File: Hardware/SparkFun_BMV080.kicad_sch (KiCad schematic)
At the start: 27 parts, among them J2 Qwiic_Vertical, J3 Conn_01x06, J4 Conn_01x01, U1 BMV080

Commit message: pre-review last second updates
-added VCC input requirements and ranges into sch
-added temp range to sch
-added pin 1 indicator silk to molex connector
-added extra GRND trace connection on pad 2 of molex connector
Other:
- note added: "VCC INPUT ON THIS DESIGN: 3.3V (due to laser sharing VCC) Otherwise... VDDIO: 1.2-3.3V VDDD: 2.5-3.3V VDDL: 3.3V VDDA: 2.5V-3.3V Operating Temperature Range: -10C to +40C"
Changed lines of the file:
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@@
+		)
+	)
+	(text "VCC INPUT ON THIS DESIGN: 3.3V (due to laser sharing VCC)\nOtherwise...\nVDDIO: 1.2-3.3V\nVDDD: 2.5-3.3V\nVDDL: 3.3V\nVDDA: 2.5V-3.3V\n\nOperating Temperature Range: -10C to +40C"
+		(exclude_from_sim no)
+		(at 16.256 31.242 0)
+		(effects
+			(font
+				(size 1.27 1.27)
+			)
+			(justify left)
 		)
 	)

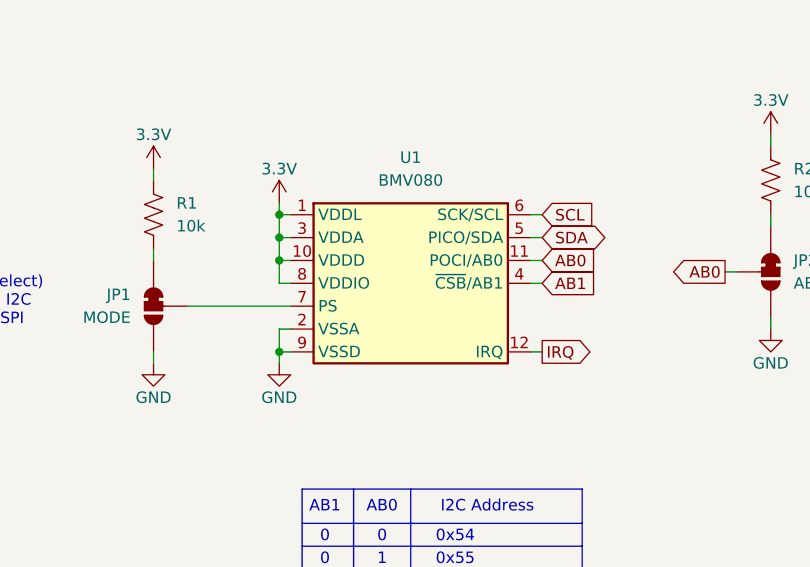
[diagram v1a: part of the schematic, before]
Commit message: sensor position outline correction and more
-added F.Fab and F.Silk outline for sensor - to help with correctly showing position on PCB
-changed PROD_ID to connector for the sensor
-made v01 in copper "knockout" style
-adjusted F.Mask to match the area of the sensor we are supposed to use thermal tape on
-adjusted B.Mask to match our small heat sink.
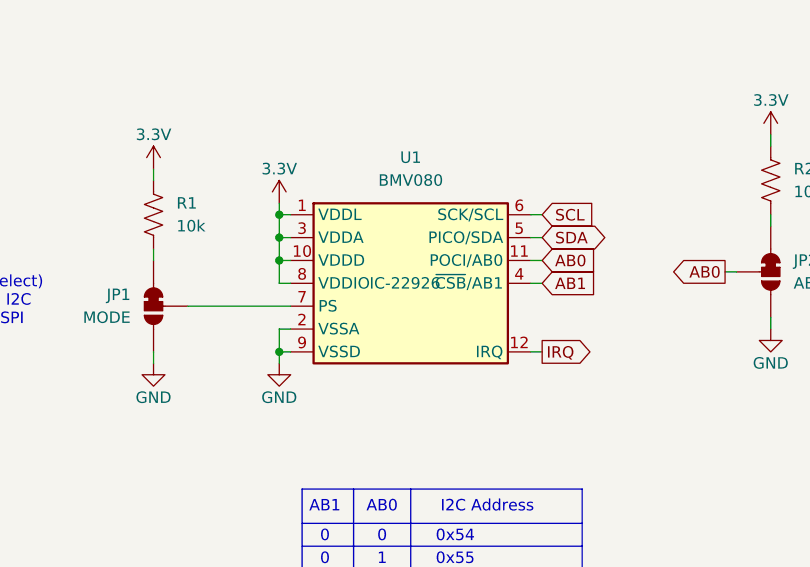
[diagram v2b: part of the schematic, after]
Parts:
- U1: PROD_ID IC-22926 -> CONN-22959; PROD_ID_SENSOR (none) -> IC-22926
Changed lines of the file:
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@@
 			)
 		)
-		(property "PROD_ID" "IC-22926"
+		(property "PROD_ID" "CONN-22959"
 			(at 91.948 102.616 0)
 			(effects
@@
 			)
 		)
+		(property "PROD_ID_SENSOR" "IC-22926"
+			(at 95.25 88.9 0)
+			(effects
+				(font
+					(size 1.27 1.27)
+				)
+			)
+		)

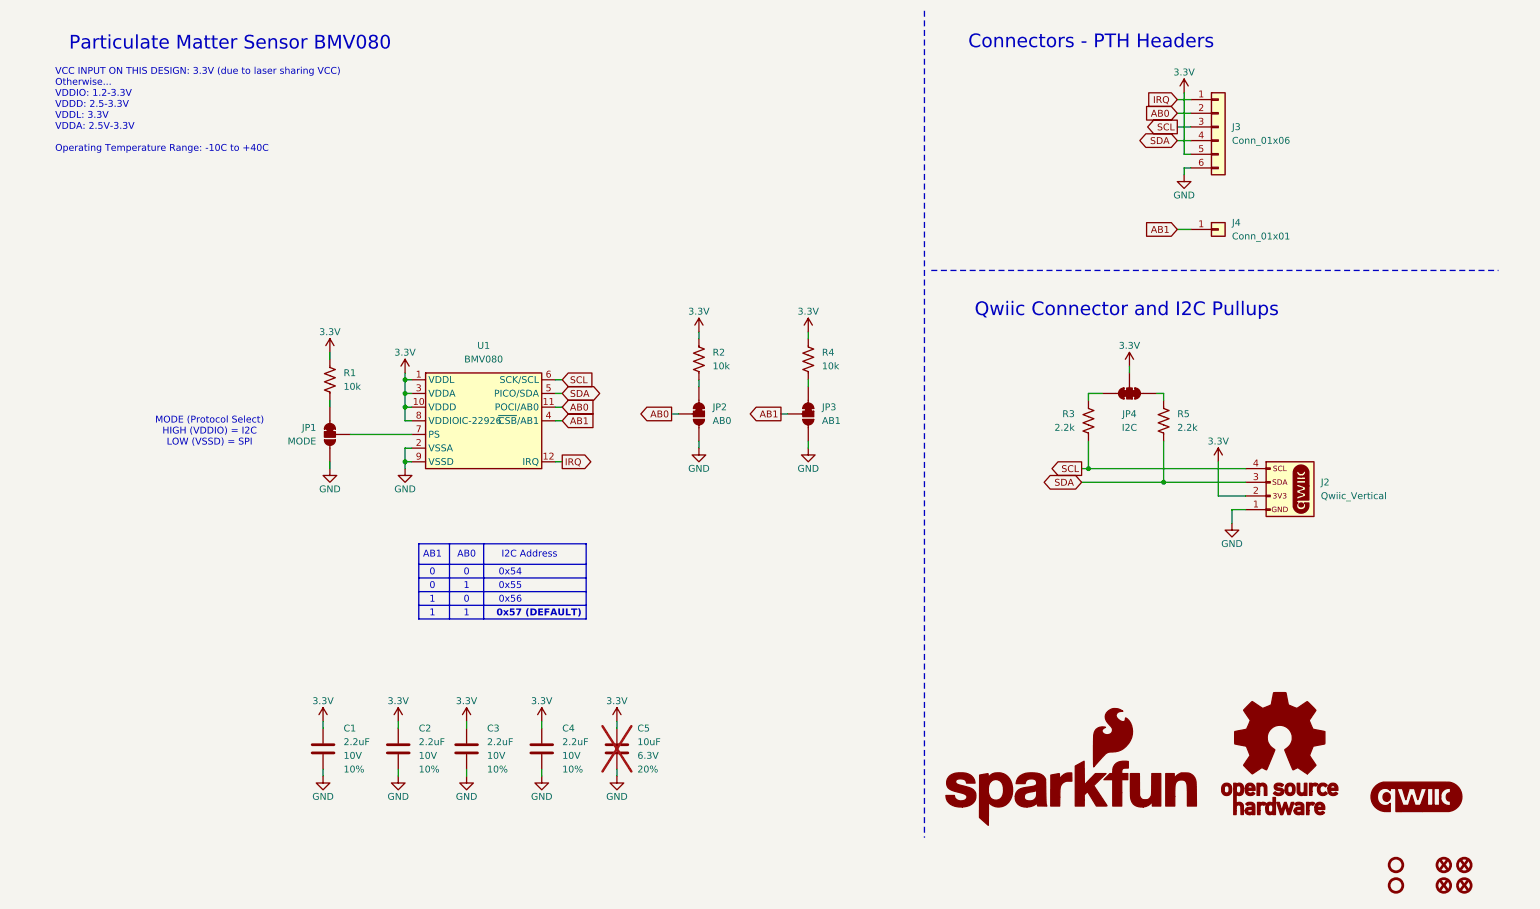
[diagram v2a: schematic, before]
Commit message: checklist run eng
-sch tightening
-sch jumpers text notes
-set solder mask expansion to 0.05mm
-added active low line on top of CS label silk
-SCL silk label set to input end flag type
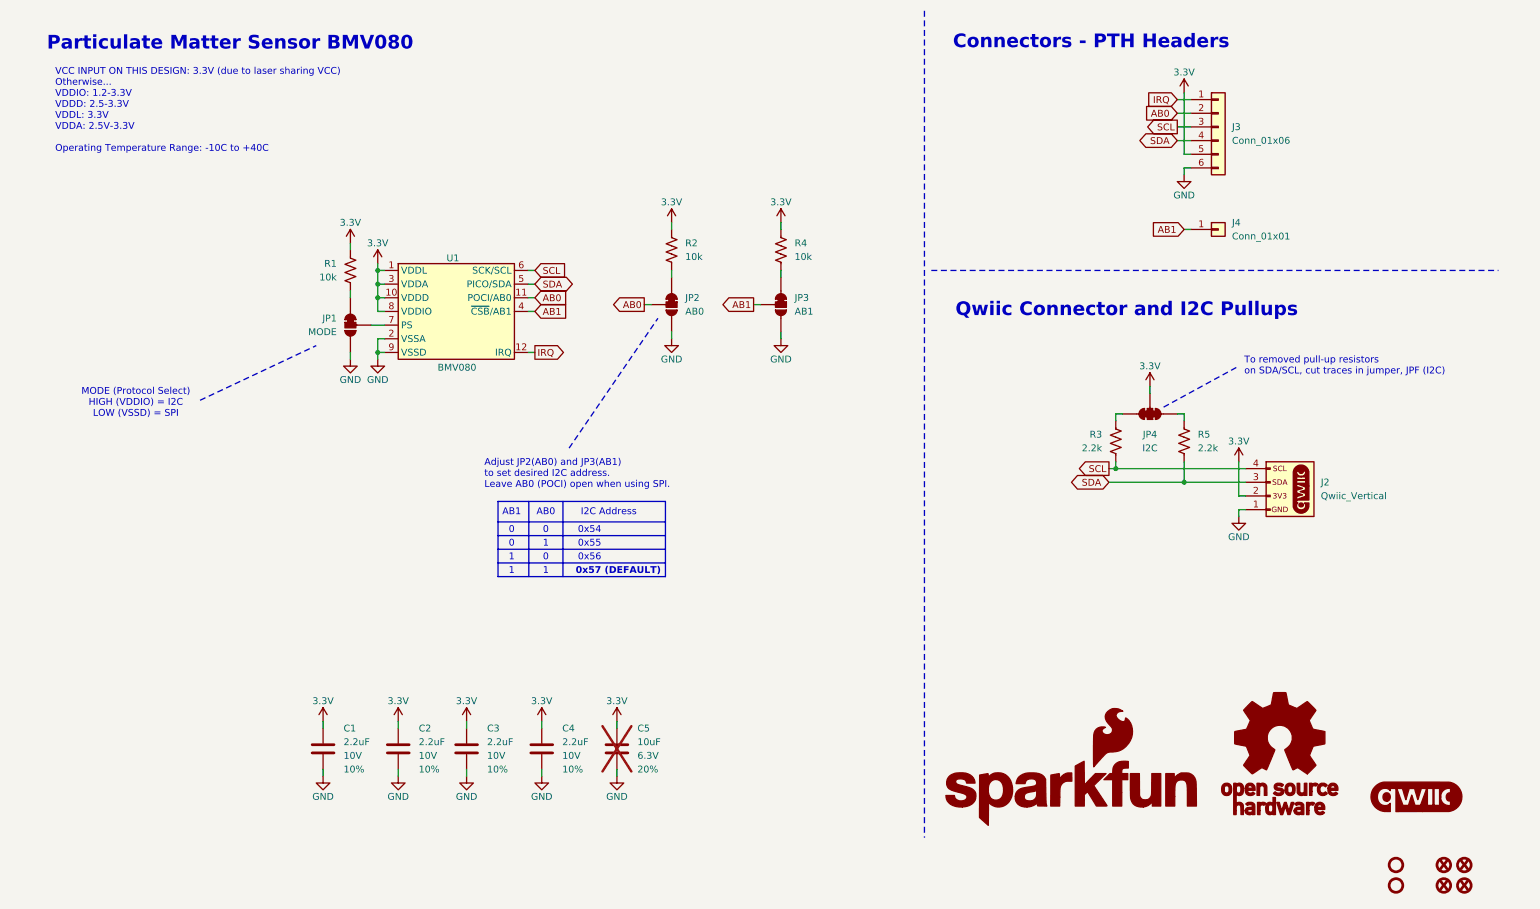
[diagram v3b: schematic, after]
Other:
- note added: "Adjust JP2(AB0) and JP3(AB1) to set desired I2C address. Leave AB0 (POCI) open when using SPI."
- note added: "To removed pull-up resistors on SDA/SCL, cut traces in jumper, JPF (I2C)"
- moved on the sheet: JP1, JP2, JP3, JP4, R1, R2, R3, R4, R5, U1

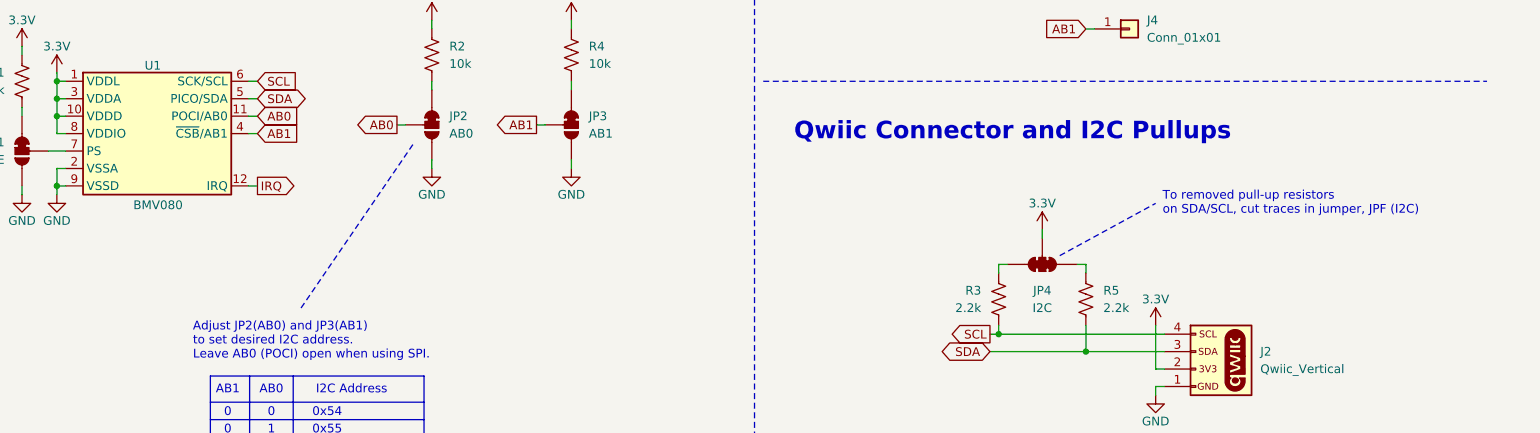
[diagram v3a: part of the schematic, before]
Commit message: -tiny tweaks before ordering v01
-updated measures on AB1 header
-updated F.FAB drawing of plastic on molex to better estimate reflow position
-moved NC into symbol box to avoid accidentally netting to it
-CSB is now CS with a line
-SCK clock silk label is round
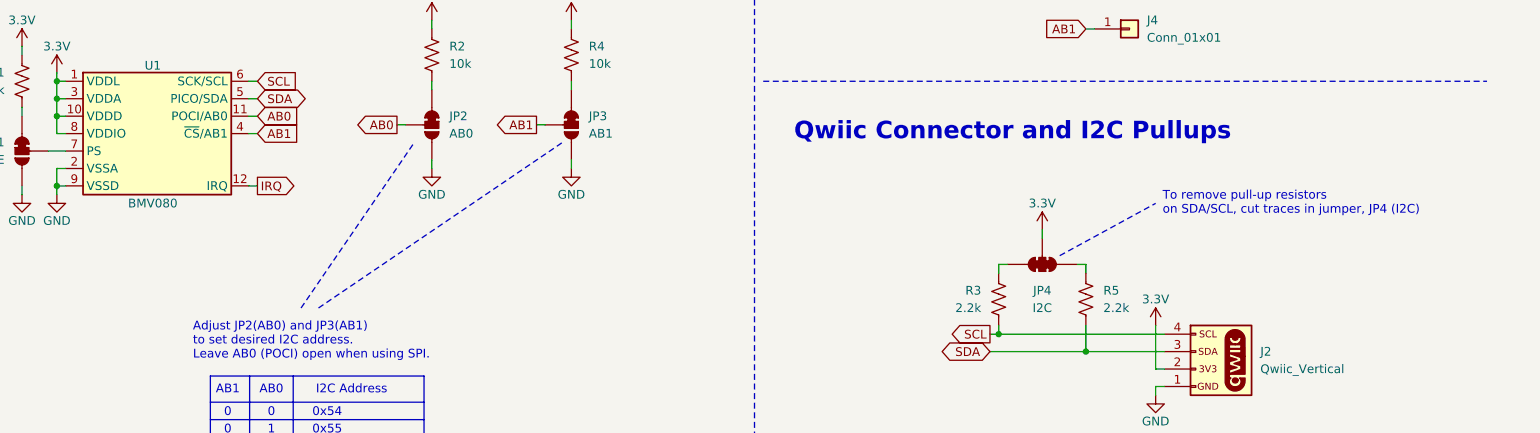
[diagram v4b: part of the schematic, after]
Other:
- note added: "To remove pull-up resistors on SDA/SCL, cut traces in jumper, JP4 (I2C)"
- note removed: "To removed pull-up resistors on SDA/SCL, cut traces in jumper, JPF (I2C)"
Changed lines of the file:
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@@
+		)
+	)
+	(polyline
+		(pts
+			(xy 114.3 93.98) (xy 149.86 69.85)
+		)
+		(stroke
+			(width 0)
+			(type dash)
+			(color 132 132 132 1)
 		)
 	)
@@
 		)
 	)
-	(text "To removed pull-up resistors\non SDA/SCL, cut traces in jumper, JPF (I2C)"
+	(text "To remove pull-up resistors\non SDA/SCL, cut traces in jumper, JP4 (I2C)"
 		(exclude_from_sim no)
 		(at 237.236 78.74 0)
@@
 		)
 		(property "Value" "BMV080"
-			(at 90.932 78.994 0)
+			(at 90.17 78.74 0)
 			(effects
 				(font
@@
 		)
 		(property "Footprint" "BMV080:FPC_0.3mm-13_molex_503566-1302"
-			(at 88.9 67.31 0)
+			(at 89.662 85.598 0)
 			(effects
 				(font
@@
 		)
 		(property "Datasheet" "NDA"
-			(at 88.9 67.31 0)
+			(at 89.408 83.566 0)
 			(effects
 				(font
@@
 		)
 		(property "Description" "BMV080 Particulate Matter Sensor"
-			(at 90.17 79.756 0)
+			(at 91.44 88.138 0)
 			(effects
 				(font
@@
 		)
 		(property "PROD_ID" "CONN-22959"
-			(at 86.868 82.296 0)
+			(at 90.424 90.17 0)
 			(effects
 				(font
@@
 		)
 		(property "PROD_ID_SENSOR" "IC-22926"
-			(at 90.17 79.502 0)
-			(effects
-				(font
+			(at 89.662 81.28 0)
+			(effects
+				(font

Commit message: v02 pcb protos v29a enclosure
-RA qwiic connector
-removed standoffs
-single pth header row now includes CS
-moved pth header upwards to clear enclosure slot
-decreased width from 1 inch to 0.95 inch
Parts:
- removed J2: Qwiic_Vertical, SparkFun-Connector:JST_SMD_1.0mm-4_Vertical, symbol SparkFun-Connector:Qwiic_Vertical
- removed J3: Conn_01x06, SparkFun-Connector:1x06, symbol SparkFun-Connector:Conn_01x06
- removed J4: Conn_01x01, SparkFun-Connector:1x01, symbol SparkFun-Connector:Conn_01x01
- removed ST1, ST2: Standoff, SparkFun-Hardware:Standoff, symbol SparkFun-Hardware:Standoff
- added J1: Qwiic_RA, SparkFun-Connector:JST_SMD_1.0mm-4_RA, symbol SparkFun-Connector:Qwiic_Right_Angle
- added J2: Conn_01x07, SparkFun-Connector:1x07, symbol SparkFun-Connector:Conn_01x07
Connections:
- net 3.3V: now also J1.2 (Pin_2), J2.5 (Pin_5)
- net AB0: now also J2.2 (Pin_2)
- net AB1: now also J2.7 (Pin_7)
- net GND: now also J1.1 (Pin_1), J2.6 (Pin_6)
- net IRQ: now also J2.1 (Pin_1)
- net SCL: now also J1.4 (Pin_4), J2.3 (Pin_3)
- net SDA: now also J1.3 (Pin_3), J2.4 (Pin_4)

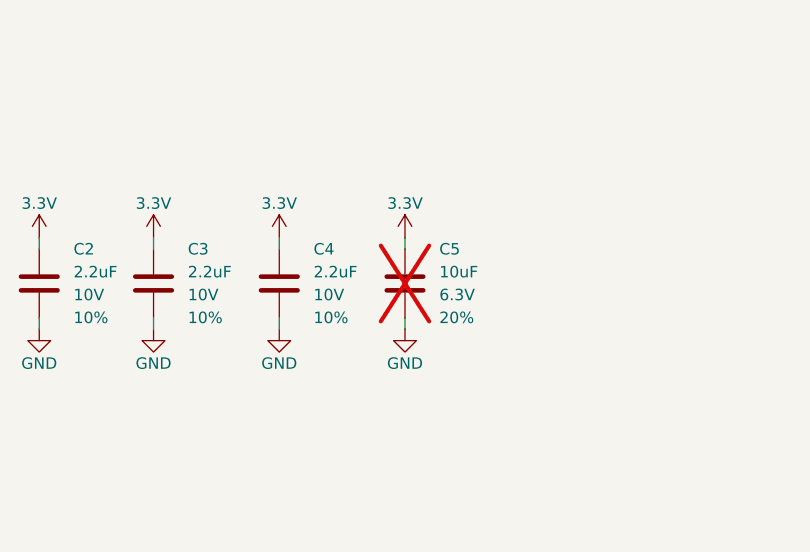
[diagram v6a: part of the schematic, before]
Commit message: Changed C5 from DNP to populated
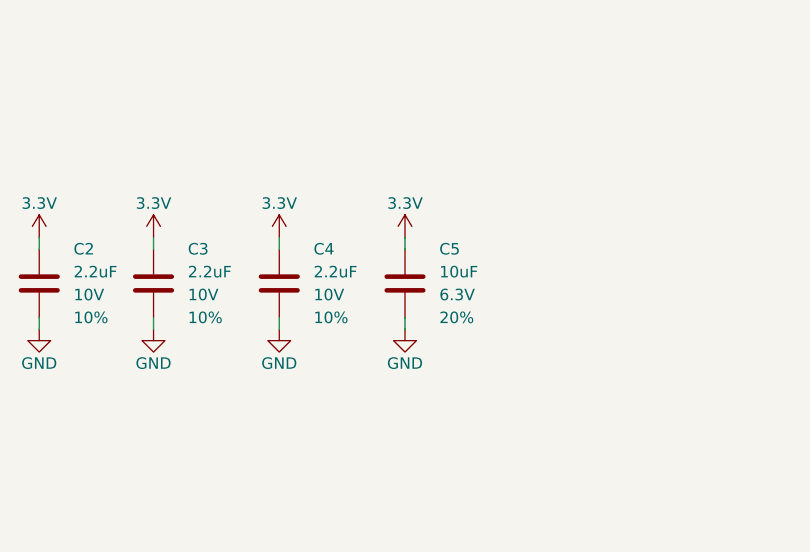
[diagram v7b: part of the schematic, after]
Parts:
- C5: now fitted
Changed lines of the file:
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@@
 		(in_bom yes)
 		(on_board yes)
-		(dnp yes)
+		(dnp no)
 		(fields_autoplaced yes)
 		(property "Reference" "C5"
